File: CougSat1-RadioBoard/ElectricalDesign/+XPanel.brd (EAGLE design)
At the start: 79 x 90 mm, 66 parts, among them J1 ADCS Connector, J2 Low Gain +, J3 Low Gain -, J4 Low Gain Coax, J5 GPS Coax, J6 EPS Connector, U1 AD8515, U3 AD7291

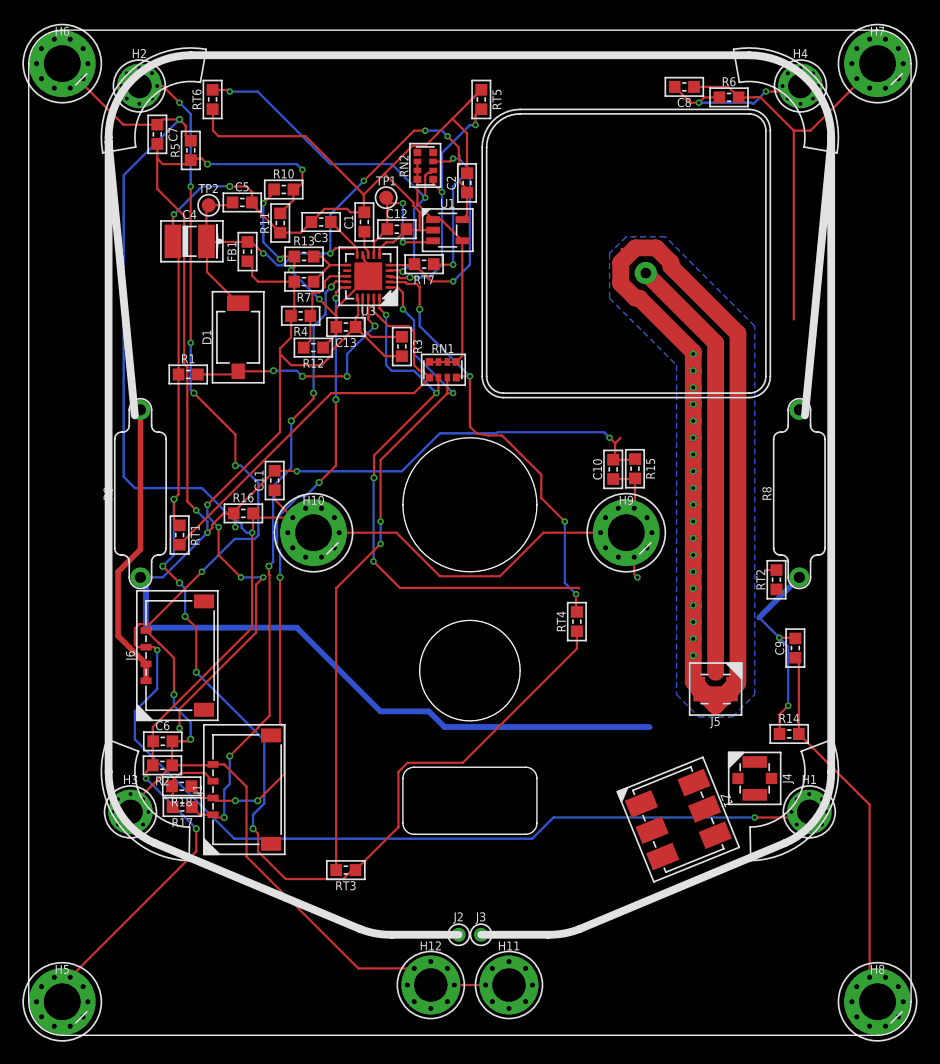
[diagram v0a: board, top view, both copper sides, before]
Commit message: Rerouted Traces
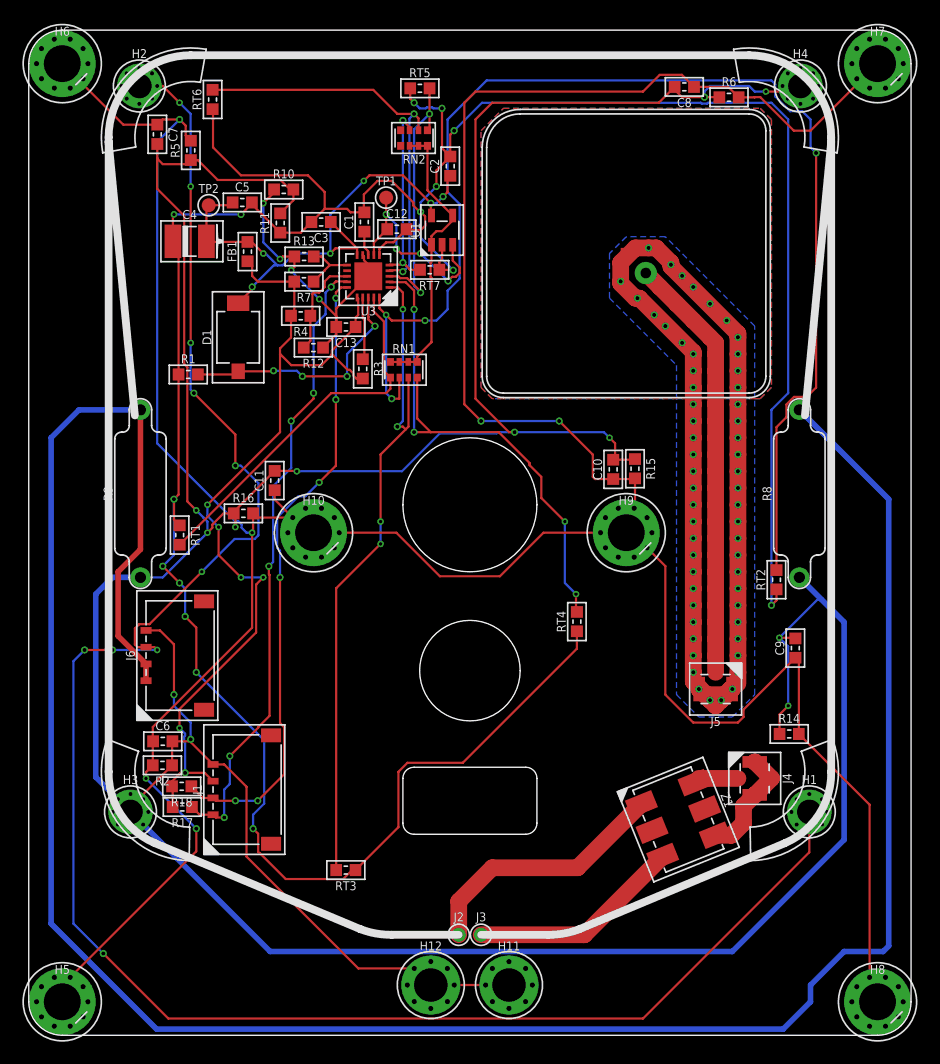
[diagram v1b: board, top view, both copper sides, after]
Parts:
- moved RT5 5.59 mm to (-4.48, 39.8), turned to 0 degrees
- moved R3 4.03 mm to (-9.59, 14.7)
- moved RN1 3.50 mm to (-5.92, 14.6)
- moved RN2 2.69 mm to (-5.00, 35.3), turned to 180 degrees
- moved C2 2.12 mm to (-1.76, 32.8)
- moved RT7 0.71 mm to (-3.60, 23.5)
- moved U1 0.50 mm to (-2.49, 27.1), turned to 90 degrees
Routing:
- net VCC: track 26.1 -> 212.8 mm
- net PGND: track 312.3 -> 425.5 mm, vias 13 -> 12
- net AGND: track 193.0 -> 263.9 mm, vias 9 -> 15
- net CHASSIS: track 372.2 -> 442.4 mm, vias 5 -> 6
- net THERM-1: track 51.1 -> 114.8 mm
- net SENSE: track 163.8 -> 200.5 mm, vias 8 -> 10
- net LOW_GAIN_P: track 0.00 -> 23.0 mm
- net LOW_GAIN_N: track 0.00 -> 19.2 mm
- net RFGND-0: track 0.00 -> 10.1 mm
- net AVDD: track 57.5 -> 50.1 mm, vias 5 -> 6
- net THERM-3: track 40.2 -> 47.2 mm
- net AVREF_UNBUF: track 13.3 -> 19.2 mm, vias 2 -> 4
- net THERM-0: track 39.0 -> 33.4 mm
- net THERM-6: track 20.8 -> 17.1 mm
- net LOW_GAIN_COAX: track 0.00 -> 3.50 mm
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- added copper zone on layer 1, net RFGND-1

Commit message: Updated RF
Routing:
- net PGND: track 425.5 -> 426.8 mm
- net LOW_GAIN_N: track 19.2 -> 20.3 mm
- net CHASSIS: track 442.4 -> 443.6 mm
- net AGND: track 263.9 -> 264.6 mm

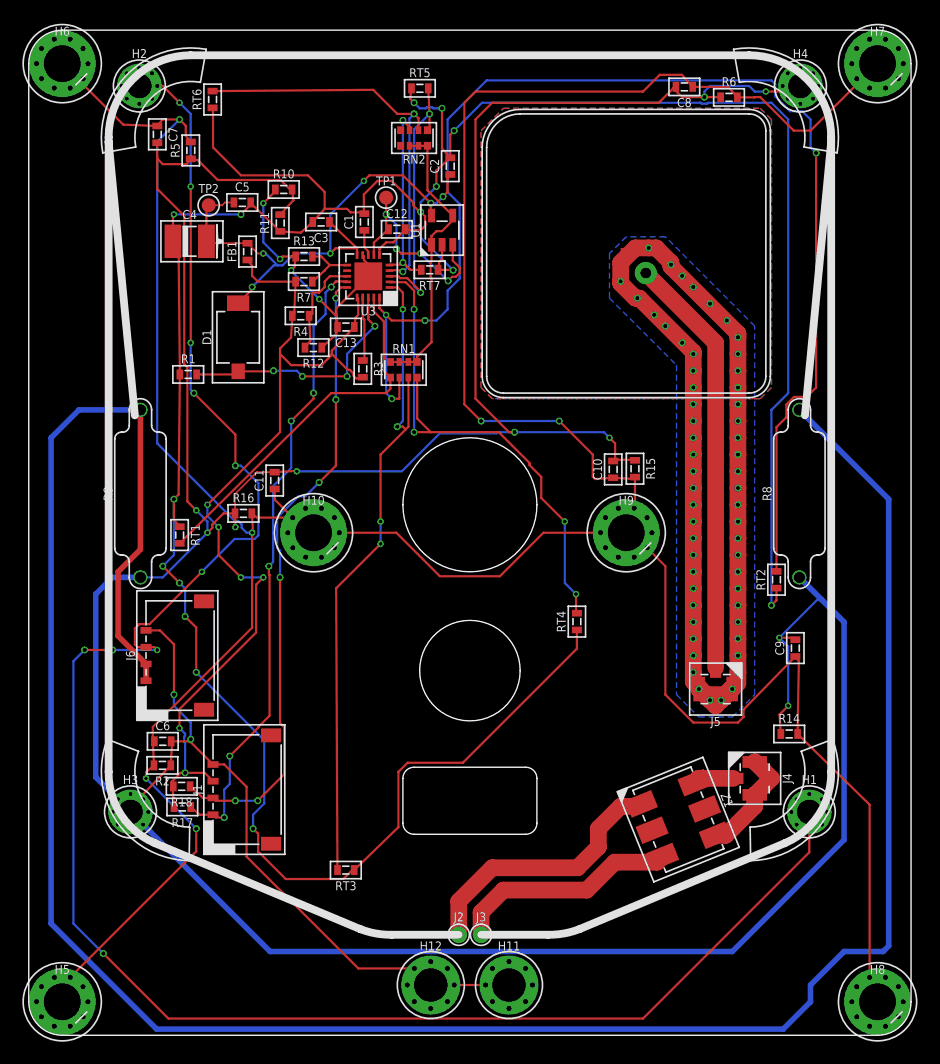
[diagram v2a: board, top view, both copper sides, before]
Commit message: Fixed RF Traces
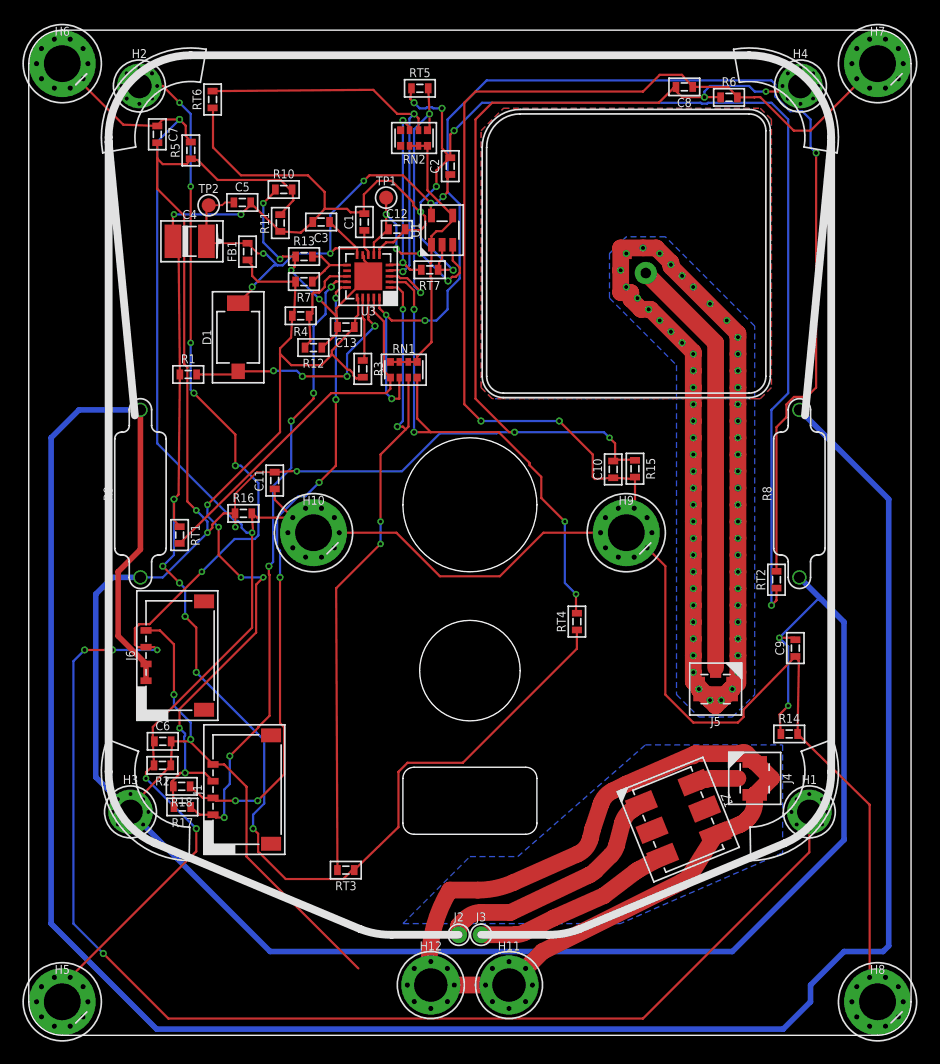
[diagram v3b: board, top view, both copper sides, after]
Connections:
- net PGND: no longer H11.1, H11.V1, H11.V2, H11.V3, H11.V4, H11.V5, H11.V6, H11.V7, H11.V8, H12.1, H12.V1, H12.V2, H12.V3, H12.V4, H12.V5, H12.V6, H12.V7, H12.V8
- net RFGND-0: now also H11.1, H11.V1, H11.V2, H11.V3, H11.V4, H11.V5, H11.V6, H11.V7, H11.V8, H12.1, H12.V1, H12.V2, H12.V3, H12.V4, H12.V5, H12.V6, H12.V7, H12.V8
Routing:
- net RFGND-0: track 9.85 -> 81.5 mm
- net PGND: track 426.8 -> 383.3 mm
- net LOW_GAIN_N: track 20.3 -> 18.1 mm
- net RFGND-1: track 94.7 -> 96.3 mm, vias 56 -> 57
- net LOW_GAIN_P: track 23.0 -> 21.8 mm
- added copper zone on layer 16, net RFGND-0

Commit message: Laid out RF
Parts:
- moved RT2 6.38 mm to (33.8, -3.21)
- moved R15 5.95 mm to (9.60, 2.80)
- moved C10 4.20 mm to (8.63, 5.67)
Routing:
- net RFGND-1: track 96.3 -> 369.1 mm, vias 57 -> 162
- net RFGND-0: track 81.5 -> 164.2 mm, vias 0 -> 41
- net PGND: track 383.3 -> 328.9 mm, vias 12 -> 11
- net SENSE: track 200.5 -> 158.0 mm
- net CHASSIS: track 443.6 -> 406.7 mm
- net AGND: track 264.6 -> 243.2 mm, vias 15 -> 14
- net THERM-1: track 115.0 -> 102.0 mm
- net LOW_GAIN_P: track 21.8 -> 20.8 mm
- added copper zone on layer 1, net GPS_COAX
- added copper zone on layer 1, net LOW_GAIN_COAX
- added copper zone on layer 1, net RFGND-0

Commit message: Fixed Airwires
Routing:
- net PGND: track 328.9 -> 372.4 mm, vias 11 -> 12
- net SENSE: track 158.0 -> 200.3 mm, vias 10 -> 11
- net CHASSIS: track 406.7 -> 447.7 mm, vias 6 -> 7
- net AGND: track 243.2 -> 261.8 mm, vias 14 -> 15
- net THERM-1: track 102.0 -> 113.0 mm

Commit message: Routed Traces
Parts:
- removed RN1, RN2: 10kΩ 1%, CougsInSpace-Resistors:1632
- added RN3: 10kΩ 5%, CougsInSpace-Resistors:3264
- moved RT6 40.3 mm to (17.3, 39.1), turned to 0 degrees
- moved C5 26.4 mm to (-20.5, 3.20)
- moved R10 23.7 mm to (-16.4, 7.00)
- moved FB1 22.8 mm to (-22.9, 2.60), turned to 270 degrees
- moved R11 22.5 mm to (-16.4, 5.20), turned to 0 degrees
- moved C4 20.5 mm to (-20.7, 6.10), turned to 180 degrees
- moved RT5 18.4 mm to (-22.9, 39.0)
- moved C10 12.5 mm to (14.9, -5.10), turned to 270 degrees
- moved D1 11.4 mm to (-9.70, 14.6), turned to 0 degrees
- moved R1 10.5 mm to (-14.9, 15.9), turned to 90 degrees
- moved C2 9.25 mm to (-11.0, 32.5), turned to 180 degrees
- moved U1 9.16 mm to (-11.3, 29.6), turned to 0 degrees
- moved TP1 8.80 mm to (-15.7, 33.2)
- moved R15 8.64 mm to (13.1, -5.10), turned to 90 degrees
- moved R12 7.10 mm to (-18.6, 22.0), turned to 90 degrees
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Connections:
- net AVREF: now also RN3.10, RN3.5; no longer RN1.5, RN1.6, RN1.7, RN1.8, RN2.6, RN2.7, RN2.8
- net THERM-0: now also RN3.6; no longer RN1.1
- net THERM-1: now also RN3.7; no longer RN1.2
- net THERM-2: now also RN3.8; no longer RN1.3
- net THERM-3: now also RN3.4; no longer RN1.4
- net THERM-4: now also RN3.3; no longer RN2.1
- net THERM-5: now also RN3.2; no longer RN2.2
- net THERM-6: now also RN3.1; no longer RN2.3
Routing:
- net SENSE: track 200.3 -> 144.5 mm, vias 11 -> 4
- net THERM-1: track 113.0 -> 76.7 mm, vias 4 -> 2
- net PGND: track 372.4 -> 337.5 mm, vias 12 -> 1
- net CHASSIS: track 447.7 -> 477.6 mm, vias 7 -> 4
- net AGND: track 261.8 -> 236.4 mm, vias 15 -> 9
- net PHOTODIODE_SENSE: track 22.2 -> 9.10 mm, vias 4 -> 0
- net AVDD: track 50.0 -> 60.5 mm, vias 6 -> 4
- net AVREF_UNBUF: track 19.2 -> 10.9 mm, vias 4 -> 2
- net THERM-5: track 36.4 -> 44.2 mm
- net THERM-0: track 33.4 -> 27.2 mm, vias 0 -> 4
- net THERM-2: track 61.2 -> 66.9 mm
- net 3.3V: track 81.4 -> 75.8 mm, vias 6 -> 2
- net ADC_AS1: track 9.20 -> 3.69 mm
- net THERM-6: track 17.2 -> 11.7 mm
- net THERM-4: track 24.1 -> 29.5 mm
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
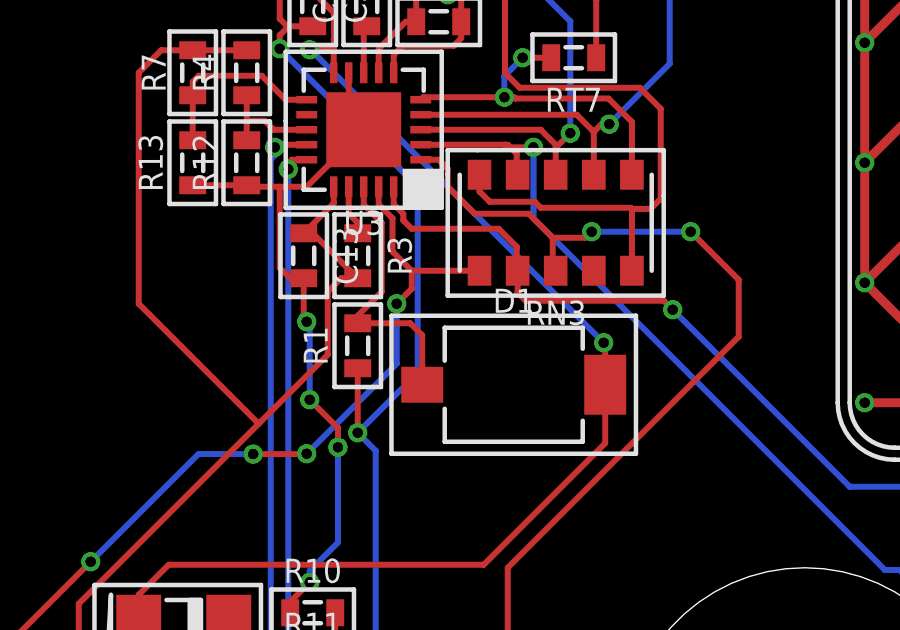
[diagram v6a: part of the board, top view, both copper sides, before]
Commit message: Modified Photodiode
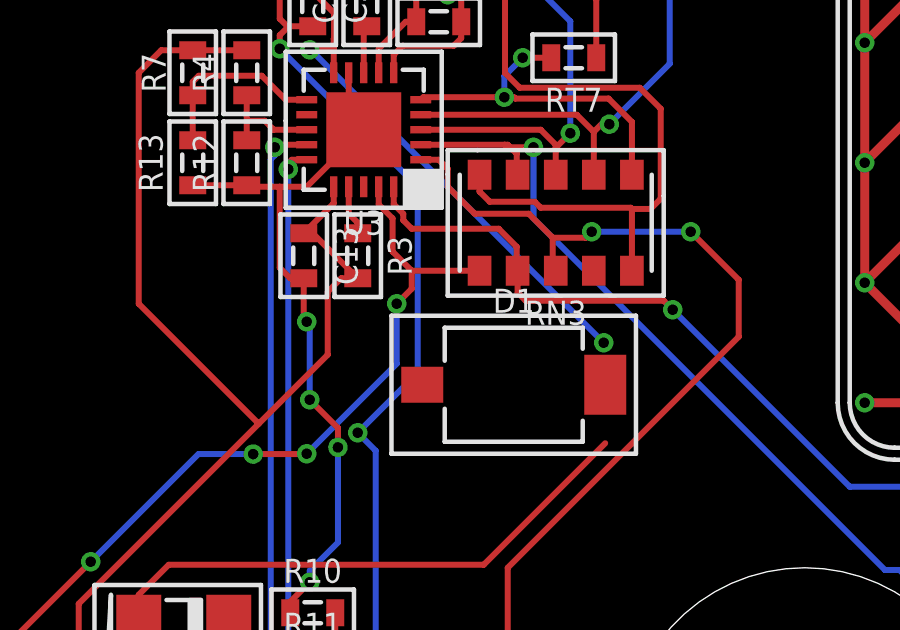
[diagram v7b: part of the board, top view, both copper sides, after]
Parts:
- removed R1: 150Ω 1%, CougsInSpace-Resistors:1608
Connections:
- removed net PHOTODIODE_SENSE: D1.A, R1.2, U3.18
- net AGND: now also D1.A; no longer R1.1
- net AVDD: no longer D1.C
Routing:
- net PHOTODIODE_SENSE: track 9.10 -> 0.00 mm
- net AVDD: track 60.5 -> 57.2 mm
- net AGND: track 236.4 -> 234.3 mm
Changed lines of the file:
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@@
 <attribute name="SKU" value="04-0001" x="-56.94" y="-30.05" size="1.778" layer="27" rot="R270" display="off"/>
-</element>
-<element name="R1" library="CougsInSpace-Resistors" package="1608" value="150Ω 1%" x="-14.9" y="15.9" smashed="yes" rot="R90">
-<attribute name="NAME" x="-16.3" y="15.9" size="0.8" layer="25" font="vector" ratio="15" rot="R90" align="center"/>
-<attribute name="PACKAGE" value="1608" x="43.52" y="61.62" size="1.778" layer="27" rot="R90" display="off"/>
-<attribute name="POWER" value="1/10W" x="43.52" y="61.62" size="1.778" layer="27" rot="R90" display="off"/>
-<attribute name="SKU" value="21-1500" x="43.52" y="61.62" size="1.778" layer="27" rot="R90" display="off"/>
-<attribute name="TEMP" value="100ppm/°C" x="43.52" y="61.62" size="1.778" layer="27" rot="R90" display="off"/>
 </element>
 <element name="R10" library="CougsInSpace-Resistors" package="1608" value="0Ω &lt;20mΩ" x="-16.4" y="7" smashed="yes">
@@
 </signal>
 <signal name="AGND">
-<contactref element="R1" pad="1"/>
 <contactref element="R11" pad="1"/>
 <contactref element="C4" pad="C"/>
@@
 <wire x1="-17.15" y1="4.15" x2="-17.15" y2="5.2" width="0.2" layer="1"/>
 <wire x1="-16.9" y1="3.9" x2="-17.15" y2="4.15" width="0.2" layer="1"/>
-<wire x1="-14.9" y1="15.15" x2="-14.9" y2="13" width="0.2" layer="1"/>
 <via x="-14.9" y="13" extent="1-16" drill="0.35"/>
 <wire x1="-14.9" y1="13" x2="-14.3" y2="12.4" width="0.2" layer="16"/>
@@
 <wire x1="-17.5" y1="26.25" x2="-17.2" y2="26.55" width="0.2" layer="1"/>
 <wire x1="-12.9" y1="15" x2="-12.9" y2="21.2" width="0.2" layer="16"/>
+<contactref element="D1" pad="A"/>
+<wire x1="-12.75" y1="14.6" x2="-12.9" y2="15" width="0" layer="19" extent="1-16"/>
 </signal>
 <signal name="AVDD">
-<contactref element="D1" pad="C"/>
 <contactref element="FB1" pad="2"/>
 <contactref element="C4" pad="A"/>
@@
 <wire x1="-16.3" y1="29" x2="-16.3" y2="28.15" width="0.2" layer="1"/>
 <wire x1="-16.3" y1="28.15" x2="-16.4" y2="28.05" width="0.2" layer="1"/>
-<wire x1="-6.65" y1="14.6" x2="-6.65" y2="12.65" width="0.2" layer="1"/>
 <wire x1="-10.7" y1="8.6" x2="-21.2" y2="8.6" width="0.2" layer="1"/>
 <wire x1="-21.2" y1="8.6" x2="-22.2" y2="7.6" width="0.2" layer="1"/>
@@
 <wire x1="-17.7" y1="30.8" x2="-16.9" y2="30.8" width="0.2" layer="1"/>
 <wire x1="-16.9" y1="30.8" x2="-16.3" y2="30.2" width="0.2" layer="1"/>
-<wire x1="-6.65" y1="14.6" x2="-6.65" y2="15.95" width="0.2" layer="1"/>
 <wire x1="-6.65" y1="15.95" x2="-6.7" y2="16" width="0.2" layer="1"/>
 <via x="-6.7" y="16" extent="1-16" drill="0.35"/>
@@
 <wire x1="-16.5" y1="25.765" x2="-16.465" y2="25.8" width="0.2" layer="1"/>
 <wire x1="-16.465" y1="25.8" x2="-15.7" y2="25.8" width="0.2" layer="1"/>
+<wire x1="-6.65" y1="12.65" x2="-6.65" y2="15.95" width="0" layer="19" extent="1-1"/>
 </signal>
 <signal name="DGND">
@@
 <wire x1="-15.2" y1="25" x2="-15.2" y2="23.6" width="0.2" layer="1"/>
 </signal>
-<signal name="PHOTODIODE_SENSE">
-<contactref element="R1" pad="2"/>
-<contactref element="D1" pad="A"/>
-<contactref element="U3" pad="18"/>
-<wire x1="-14.9" y1="16.65" x2="-14.9" y2="16.9" width="0.2" layer="1"/>
-<wire x1="-14.9" y1="16.9" x2="-14.1" y2="17.7" width="0.2" layer="1"/>
-<wire x1="-14.1" y1="17.7" x2="-14.1" y2="20" width="0.2" layer="1"/>
-<wire x1="-14.1" y1="20" x2="-14.7" y2="20.6" width="0.2" layer="1"/>
-<wire x1="-14.7" y1="20.6" x2="-14.7" y2="21.2" width="0.2" layer="1"/>
-<wire x1="-12.75" y1="14.6" x2="-12.75" y2="16.25" width="0.2" layer="1"/>
-<wire x1="-13.15" y1="16.65" x2="-14.9" y2="16.65" width="0.2" layer="1"/>
-<wire x1="-12.75" y1="16.25" x2="-13.15" y2="16.65" width="0.2" layer="1"/>
-</signal>
 <signal name="I2C_SDA_ADCS">

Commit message: Fixed Traces
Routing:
- net AGND: track 234.3 -> 224.1 mm
- net THERM-2: track 66.9 -> 63.8 mm, vias 4 -> 2
- net THERM-5: track 44.2 -> 46.9 mm
- net 3.3V: track 75.8 -> 74.6 mm
- net AVDD: track 57.2 -> 58.4 mm
- net AVREF: track 25.7 -> 25.0 mm
- net DGND: track 24.5 -> 25.1 mm
